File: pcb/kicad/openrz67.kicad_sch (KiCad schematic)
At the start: 59 parts, among them U1 ESP32-C3FH4, U3 LGS5500EP, U4 S4B-XH-A(LF)(SN), U5 TLP172AM, U6 TLP172AM, X1 40MHz, X2 32.768kHz

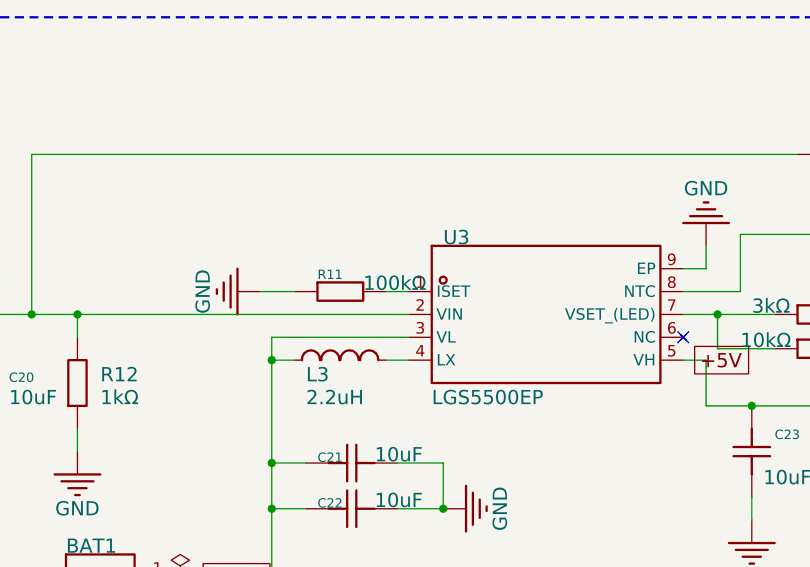
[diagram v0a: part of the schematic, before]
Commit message: PCB rev 2: apply pre-fab review fixes
Blockers from the 2026-09-07 review:
- R11 100k -> 10k. It sets the LGS5500 charge current; 100k meant 1 A into
  the 250 mAh cell (rev 1 shipped like that). 10k = 400 mA per datasheet.
- Three resistor lines had 19-40 pieces in JLCPCB stock: 10k group ->
  C25744 (Basic), R12 1k -> C21190 (Basic), R18 3k -> C2909355. Library
  symbols renamed to the new MPNs, 100k symbol dropped, board fields synced.
- The VCC via feeding L2 pad 1 had its hole 0.083 mm inside the pad copper;
  moved 0.55 mm below the pad with a short F.Cu stub.

Should-fixes:
- openrz67.kicad_dru: two scoped rules instead of one unscoped one, so the
  pours stay 0.25 mm off the USB1 peg holes (rev-1 geometry) while USB1's
  own pads keep 0.17 mm.
- regen.sh: gerbers and drill use the aux origin like the CPL, so the drill
  files diff directly against the rev-1 archive; CPL rotations 0-359;
  BOM written with JLCPCB's column names and no library prefix.
- S1_DRV via nudged 0.15 mm off U1 pad 9; VDDA added to the 3v net class.

DRC 0 errors / 9 known warnings, ERC 0/0, parity clean. Every non-via
drill hole matches the rev-1 archive.
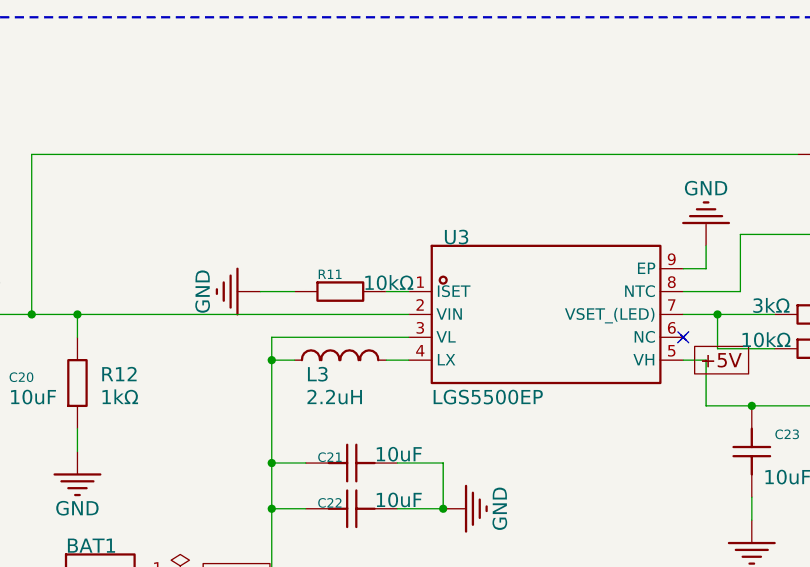
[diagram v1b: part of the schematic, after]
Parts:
- R11: value 100kΩ -> 10kΩ; symbol openrz67:0402WGF1003TCE -> openrz67:0402WGF1002TCE; LCSC Part Name 100kΩ ±1% 62.5mW 厚膜电阻 -> 10kΩ ±1% 62.5mW 厚膜电阻; Manufacturer Part 0402WGF1003TCE -> 0402WGF1002TCE; Supplier Part C25741 -> C25744
- R12: symbol openrz67:0603WAJ0102T5E -> openrz67:0603WAF1001T5E; LCSC Part Name 1kΩ ±5% 100mW 厚膜电阻 -> 1kΩ ±1% 100mW 厚膜电阻; Manufacturer Part 0603WAJ0102T5E -> 0603WAF1001T5E; Supplier Part C25585 -> C21190
- R13, R14, R17, R20, R6, R7, R8: symbol openrz67:RC0402FR-0710KL -> openrz67:0402WGF1002TCE; LCSC Part Name 厚膜电阻 10kΩ ±1% 62.5mW -> 10kΩ ±1% 62.5mW 厚膜电阻; Manufacturer YAGEO(国巨) -> UNI-ROYAL(厚声); Manufacturer Part RC0402FR-0710KL -> 0402WGF1002TCE; Supplier Part C60490 -> C25744
- R18: symbol openrz67:0603WAF3001T5E -> openrz67:FRC0402F3001TS; Manufacturer UNI-ROYAL(厚声) -> FOJAN; Manufacturer Part 0402WGF3001TCE -> FRC0402F3001TS; Supplier Part C25784 -> C2909355

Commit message: PCB: unpopulated 1x4 GPIO header J1 along the bottom edge
3V3, GND, GPIO21 (U0TXD, doubles as UART TX for logging) and GPIO6 on
2.54 mm through-hole pads at x = 34.4-42.0, y = 20.3 mm, below the AGND
island so camera isolation is untouched. J1 is DNP in the schematic and on
the board, so --exclude-dnp keeps it out of the BOM and CPL; the pads are
just copper and holes on the bare PCB.

Only one right-column ESP32-C3 pin fits through the gap between the VCC,
CHIP_EN and S2_DRV tracks, the same limit the 2026-09-03 header attempt
hit; GPIO6 took it, GPIO21 escapes from the left column. Two GND stitching
vias under the pads were removed and one added at (32.8, 17.6) to reconnect
the F.Cu strip the tracks cut off. GPIO6's B.Cu detour leaves a ~57 mm2
via-stitched ground island east of U1; the flood under U1 is intact.

Footprint copied from KiCad's Connector_PinHeader_2.54mm library (3D model
reference dropped); Conn_01x04 symbol added to the project library.
DRC 0 errors / 9 known warnings, ERC 0/0, parity clean.
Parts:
- added J1: GPIO header, openrz67:PinHeader_1x04_P2.54mm_Vertical, symbol openrz67:Conn_01x04
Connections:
- net GND: now also J1.2 (Pin_2)
- net VCC: now also J1.1 (Pin_1)
- net GPIO6: now reaches U1.12 (MTCK)
- net GPIO6: now also J1.4 (Pin_4)
- net GPIO21: now reaches U1.28 (U0TXD)
- net GPIO21: now also J1.3 (Pin_3)
- no-connect marks 18 -> 16

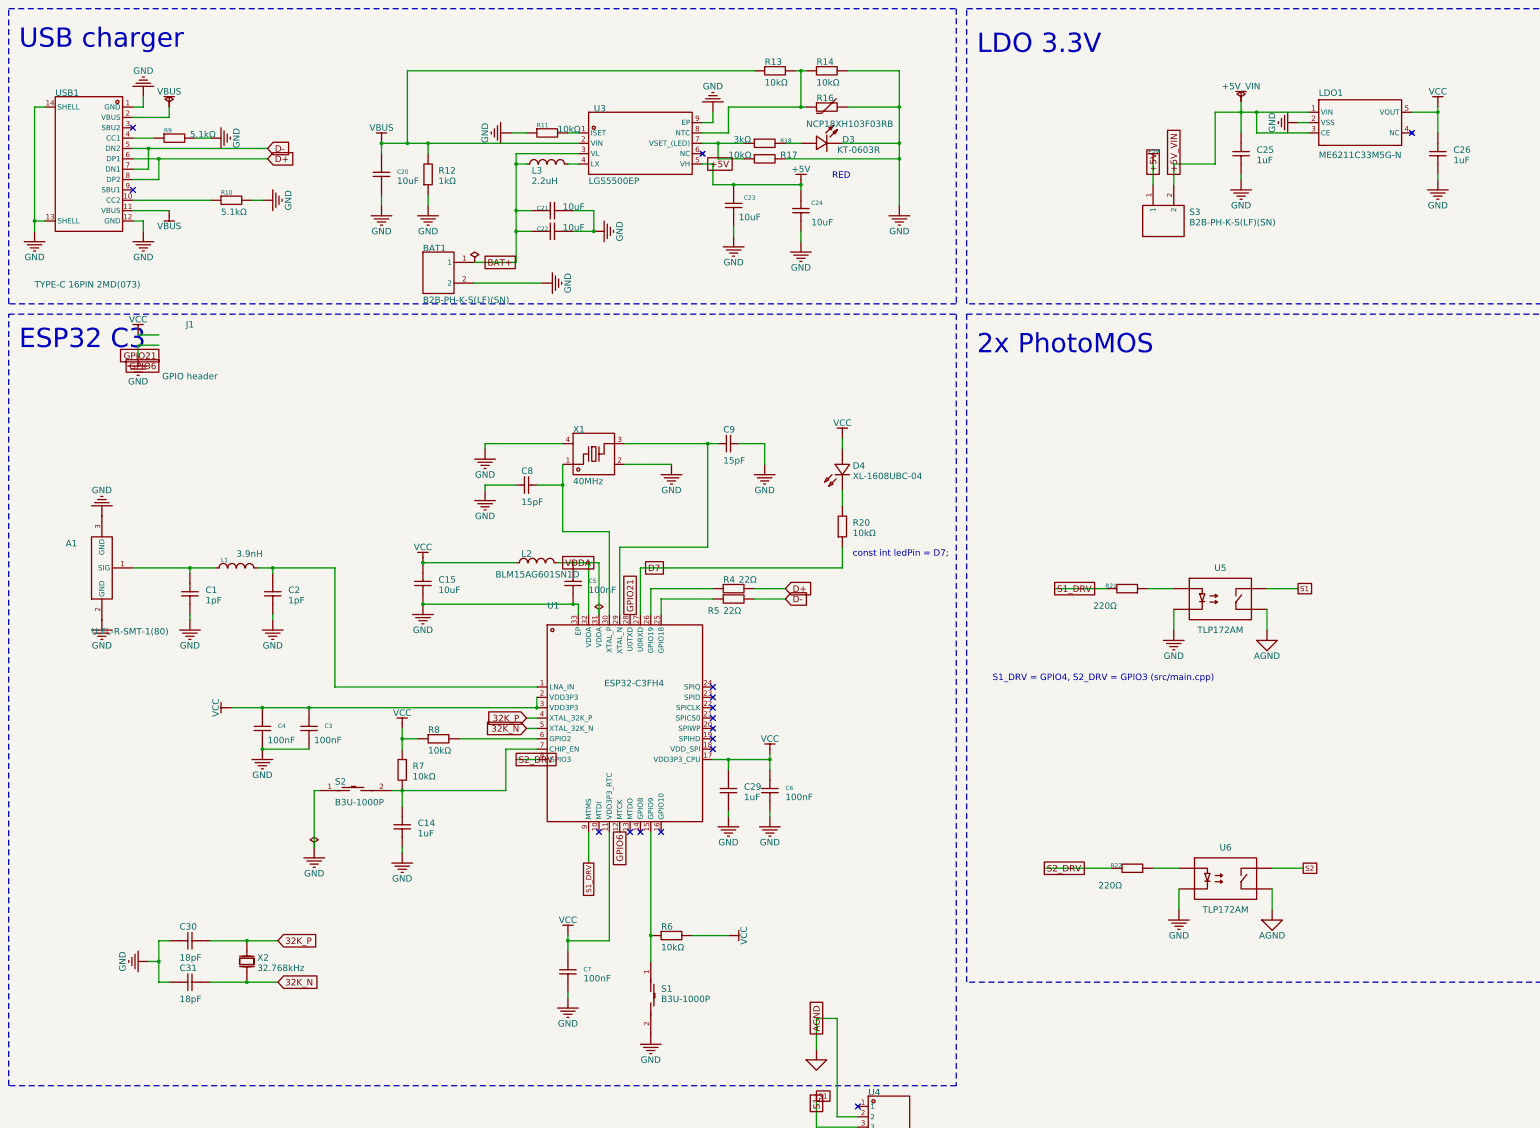
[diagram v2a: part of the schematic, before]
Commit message: PCB rev 2: BQ25185 charger + TPS63031 buck-boost replace LGS5500 + LDO
The cell is rated for 120 mA charge current; the LGS5500's lowest setting is
400 mA and rev 1 shipped at 1 A. U3 is now a BQ25185DLHR (linear charger with
power path): R11 2.7 k on ISET -> 111 mA nominal, R13 18 k on ILIM/VSET -> 500 mA
input limit / 4.20 V / 3.0 V precharge, R16 NTC on TS/MR, STAT2 drives D3 (lit
while charging). SYS feeds S3 and then U2, a TPS63031DSKR fixed 3.3 V buck-boost
that replaces the ME6211 LDO (L3 2.2 uH reused, C23/C24 10 uF, C25 100 nF VINA).
LDO1, R12, R14, R17 and the +5V nets are gone. Cross-checked against the TI
datasheets; the LCSC footprints were compared with TI's land patterns.

R21/R22 220 -> 150 ohm: PhotoMOS LED current 8.2 mA worst case instead of
5.6 mA, which sat on the 5 mA minimum the 2 ohm on-resistance is specified at.

Layout cleanup after the swap: stray LCSC fields off the silkscreen, L3 net
labels matched to the routed board, U3 STAT1 pad net, L3 moved 0.25 mm off
U2's pads, GND stub to U2 pad 9, new footprints synced to the library, zones
refilled with the DRU rules. DRC 0 errors / 14 known warnings, ERC 0 errors.

CPL: ROT_FIX in regen.sh adds +90 deg for the QFN-32 (U1) and the TLP172AM
SO-4 (U5/U6), whose JLCPCB library orientation is 90 deg off the KiCad footprint
per their order preview. The rev-1 order had the same U1 offset and JLCPCB
corrected it against the silkscreen; sending the corrected angle leaves them
nothing to fix. Verify U1/U5/U6 in the preview and the DFM analysis.
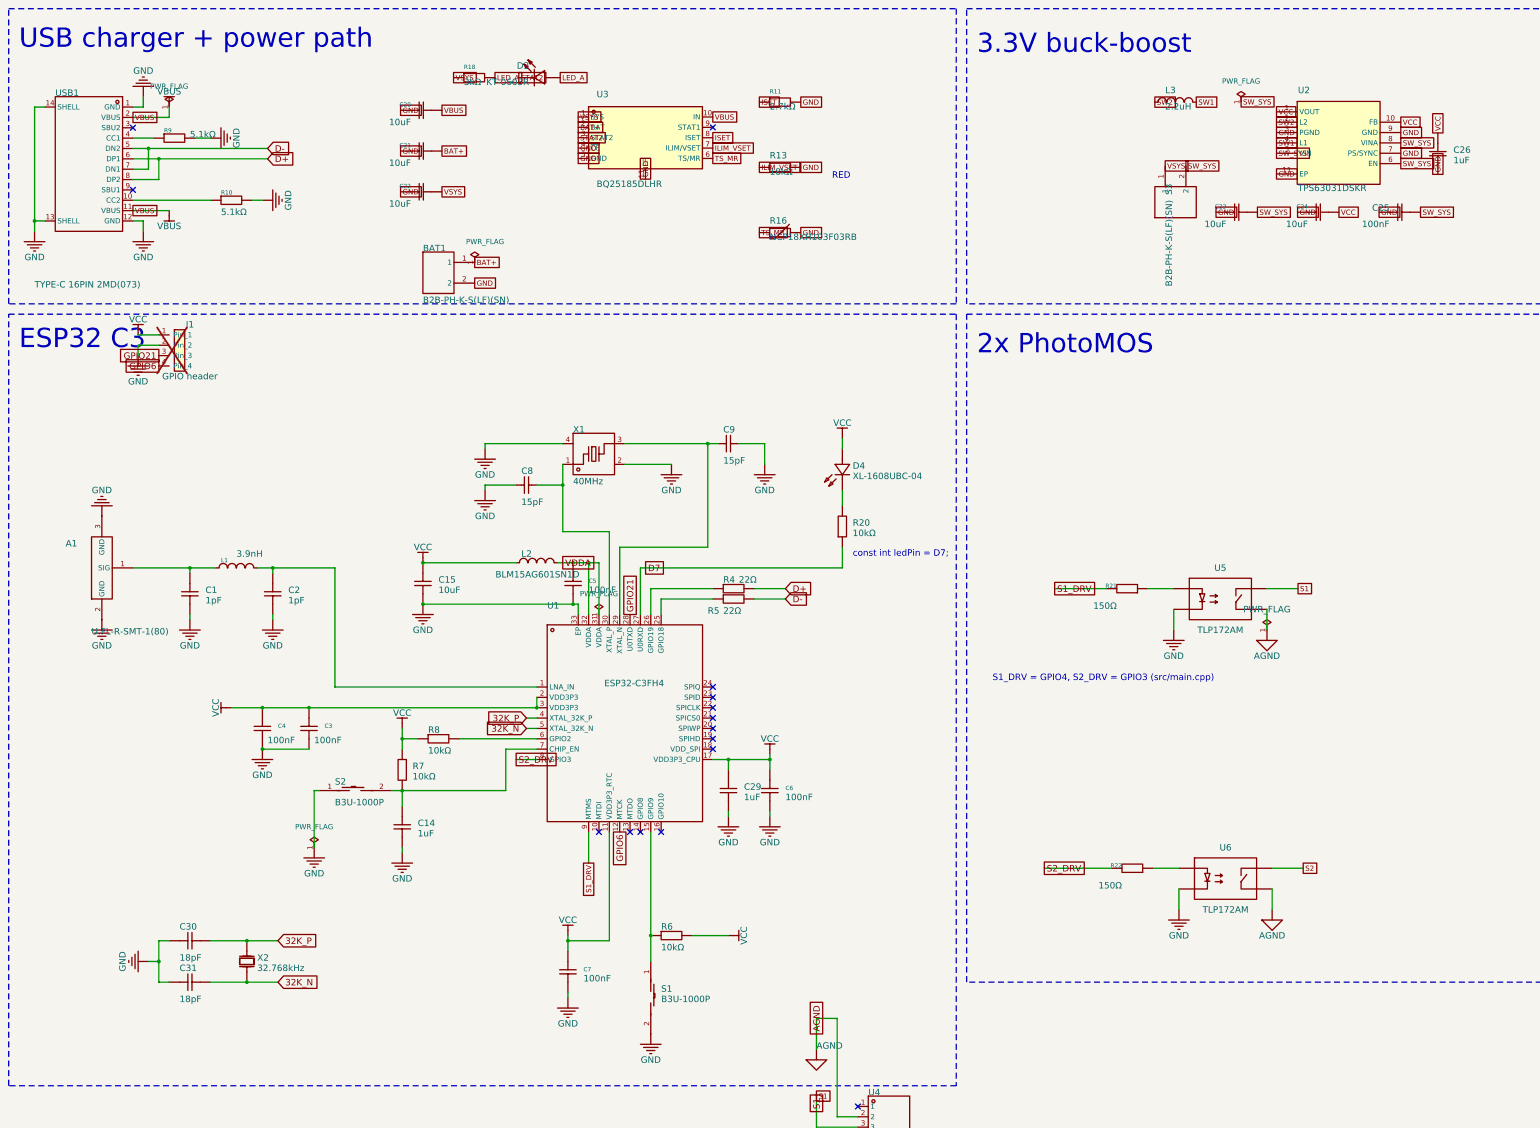
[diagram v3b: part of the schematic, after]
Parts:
- removed R12: 1kΩ, openrz67:R0603, symbol openrz67:0603WAF1001T5E
- removed R14, R17: 10kΩ, openrz67:R0402, symbol openrz67:0402WGF1002TCE
- C25: value 1uF -> 100nF; footprint openrz67:C0603 -> openrz67:C0402; symbol openrz67:CGA0603X5R105K500JT -> openrz67:GRM155R71H104KE14D; LCSC Part Name 1uF ±10% 50V -> 100nF ±10% 50V; Manufacturer HRE(芯声) -> muRata(村田); Manufacturer Part CGA0603X5R105K500JT -> GRM155R71H104KE14D; Supplier Part C6119852 -> C77020
- R11: value 10kΩ -> 2.7kΩ; symbol openrz67:0402WGF1002TCE -> openrz67:0402WGF2701TCE; LCSC Part Name 10kΩ ±1% 62.5mW 厚膜电阻 -> 2.7kΩ ±1% 62.5mW; Manufacturer Part 0402WGF1002TCE -> 0402WGF2701TCE; Supplier Part C25744 -> C25885
- R13: value 10kΩ -> 18kΩ; symbol openrz67:0402WGF1002TCE -> openrz67:0402WGF1802TCE; LCSC Part Name 10kΩ ±1% 62.5mW 厚膜电阻 -> 18kΩ ±1% 62.5mW; Manufacturer Part 0402WGF1002TCE -> 0402WGF1802TCE; Supplier Part C25744 -> C25762
- R21, R22: value 220Ω -> 150Ω; symbol openrz67:0402WGF2200TCE -> openrz67:0402WGF1500TCE; LCSC Part Name 220Ω ±1% 62.5mW 厚膜电阻 -> 150Ω ±1% 62.5mW 厚膜电阻; Manufacturer Part 0402WGF2200TCE -> 0402WGF1500TCE; Supplier Part C25091 -> C25082
- U2: renamed from LDO1; value ME6211C33M5G-N -> TPS63031DSKR; footprint openrz67:SOT-23-5_L3.0-W1.7-P0.95-LS2.8-BL -> openrz67:VSON-10_L2.5-W2.5-P0.50-EP1.2x2.0; symbol openrz67:ME6211C33M5G-N -> openrz67:TPS63031DSKR; LCSC Part Name 输入6V 输出3.3V 500mA -> TPS63031DSKR; Manufacturer MICRONE(南京微盟) -> Texas Instruments; Manufacturer Part ME6211C33M5G-N -> TPS63031DSKR; Supplier Part C82942 -> C15516
- U3: value LGS5500EP -> BQ25185DLHR; footprint openrz67:ESOP-8_L4.9-W3.9-P1.27-LS6.0-TL-EP3.3 -> openrz67:WSON-10_L2.2-W2.0-P0.40-EP0.9x1.5; symbol openrz67:LGS5500EP -> openrz67:BQ25185DLHR; LCSC Part Name 1A充电,0.3A同步升压放电,超低待机2uA+的TP5400,ETA9697 -> BQ25185DLHR; Manufacturer Legend-Si(棱晶半导体) -> Texas Instruments; Manufacturer Part LGS5500EP -> BQ25185DLHR; Supplier Part C5280699 -> C19725033
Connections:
- net BAT+: now also U3.2 (BAT); no longer C22.2, L3.1, U3.3 (VL)
- net GND: now also R11.2, R13.2, U2.11 (EP), U2.3 (PGND), U2.7 (PS/SYNC), U2.9 (GND), U3.11 (EP), U3.4 (~{CE}), U3.5 (GND); no longer D3.1 (K), R11.1, U2.2 (VSS), U3.9 (EP)
- net VBUS: now also U3.10 (IN); no longer R13.1, U3.2 (VIN)
- net VCC: now also C24.2, U2.1 (VOUT), U2.10 (FB); no longer U2.5 (VOUT)
- net LED_A: now reaches D3.2 (A), R18.2
- net VSYS: now reaches U3.1 (SYS)
- net VSYS: now also C22.2, R18.1, S3.1; no longer R11.2
- net SW1: now reaches L3.2
- net SW1: now also U2.4 (L1); no longer U3.4 (LX)
- net TS_MR: now reaches U3.6 (TS/MR)
- net TS_MR: now also R16.1
- net ILIM_VSET: now reaches U3.7 (ILIM/VSET)
- net ILIM_VSET: now also R13.1; no longer R18.1
- removed net +5V: C23.2, C24.2, S3.1, U3.5 (VH)
- net +5V_VIN renamed SW_SYS
- net SW_SYS: now also C23.2, U2.5 (VIN), U2.6 (EN), U2.8 (VINA); no longer U2.1 (VIN), U2.3 (CE)
- new net ISET: R11.1, U3.8 (ISET)
- new net STAT2: D3.1 (K), U3.3 (STAT2)
- new net SW2: L3.1, U2.2 (L2)
- no-connect marks 16 -> 15
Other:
- note added: "3.3V buck-boost"
- note added: "USB charger + power path"
- note removed: "LDO 3.3V"
- note removed: "USB charger"
- moved on the sheet: C20, C21, C22, C23, C24, C25, D3, L3, R11, R13, R16, R18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
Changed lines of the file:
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@@
-(kicad_sch
-	(version 20260306)
-	(generator "eeschema")
-	(generator_version "10.0")
-	(paper "User" 420.624 297.434)
-	(title_block
-		(title "OpenRZ67 camera trigger")
-		(date "2026-09-03")
-		(rev "2")
-		(comment 1 "Ported from EasyEDA Pro project ESP32C3CameraTrigger 2026-09-02 (rev with side-entry U4)")
-	)
+(kicad_sch (version 20260306) (generator eeschema)
+  (paper "User" 420.624 297.434)
+  (title_block
+    (title "OpenRZ67 camera trigger")
+    (date "2026-09-03")
+    (rev "2")
+    (comment 1 "Ported from EasyEDA Pro project ESP32C3CameraTrigger 2026-09-02 (rev with side-entry U4)")
+  )

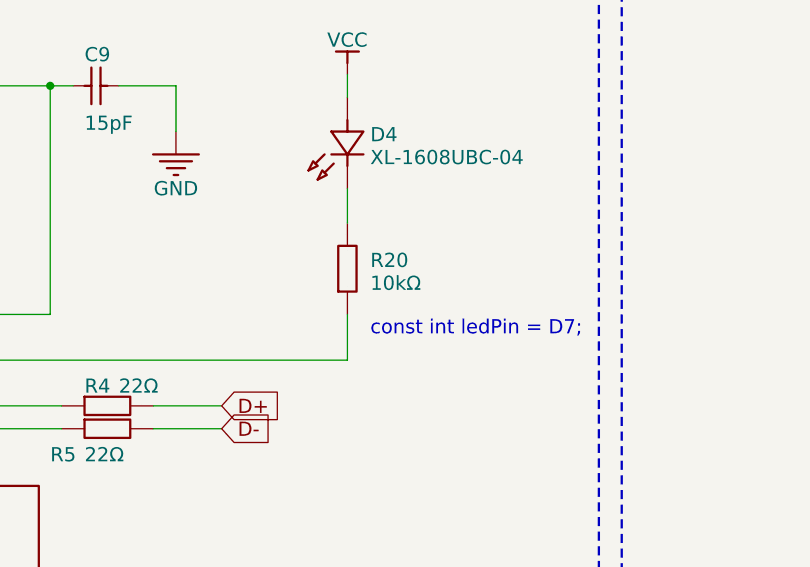
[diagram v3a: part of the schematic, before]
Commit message: PCB: R20 1 kOhm, J1 excluded from BOM/CPL by attribute, 3D model fixes, MPN
- R20 10k -> 1k (C11702): the blue status LED was practically invisible.
- J1: in_bom no on the symbol, exclude_from_bom/exclude_from_pos_files on the
  footprint, so the exclusion no longer hinges on --exclude-dnp.
- TLP172AM MPN 'TLP172AM(TPL,E' -> 'TLP172AM(TPL,E)'.
- 3D models: the imported offsets put U4 3.45 mm off and 3.4 mm low, BAT1/S3
  0.6 mm off and 3.5 mm low, USB1 1.2 mm off and 0.9 mm low (checked against the
  pin geometry in the .wrl files). Corrected in the library and the board; the
  BQ25185 and TPS63031 got their LCSC models.
DRC 0 errors / 14 known warnings, ERC 0 errors.
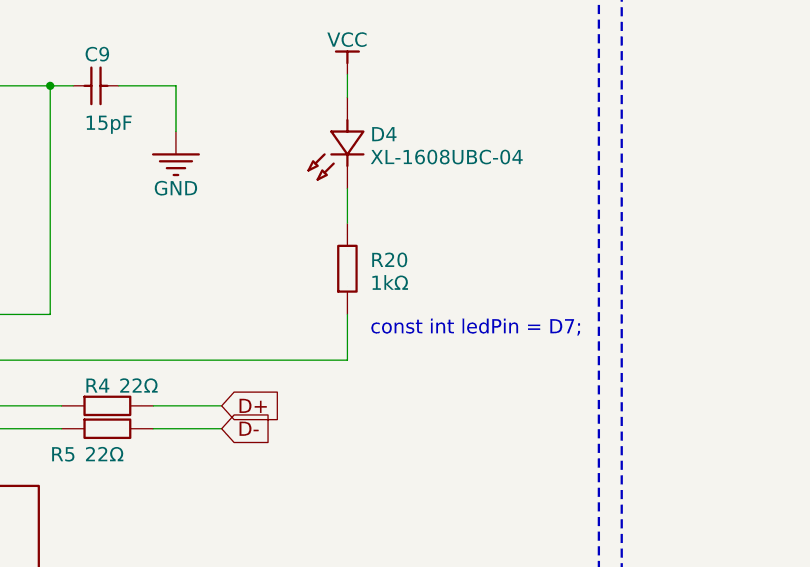
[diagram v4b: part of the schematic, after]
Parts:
- J1: now left out of the parts list
- R20: value 10kΩ -> 1kΩ; symbol openrz67:0402WGF1002TCE -> openrz67:0402WGF1001TCE; LCSC Part Name 10kΩ ±1% 62.5mW 厚膜电阻 -> 1kΩ ±1% 62.5mW; Manufacturer Part 0402WGF1002TCE -> 0402WGF1001TCE; Supplier Part C25744 -> C11702
- U5, U6: LCSC Part Name TLP172AM(TPL,E -> TLP172AM(TPL,E); Manufacturer Part TLP172AM(TPL,E -> TLP172AM(TPL,E)
